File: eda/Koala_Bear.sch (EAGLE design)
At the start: 21 parts

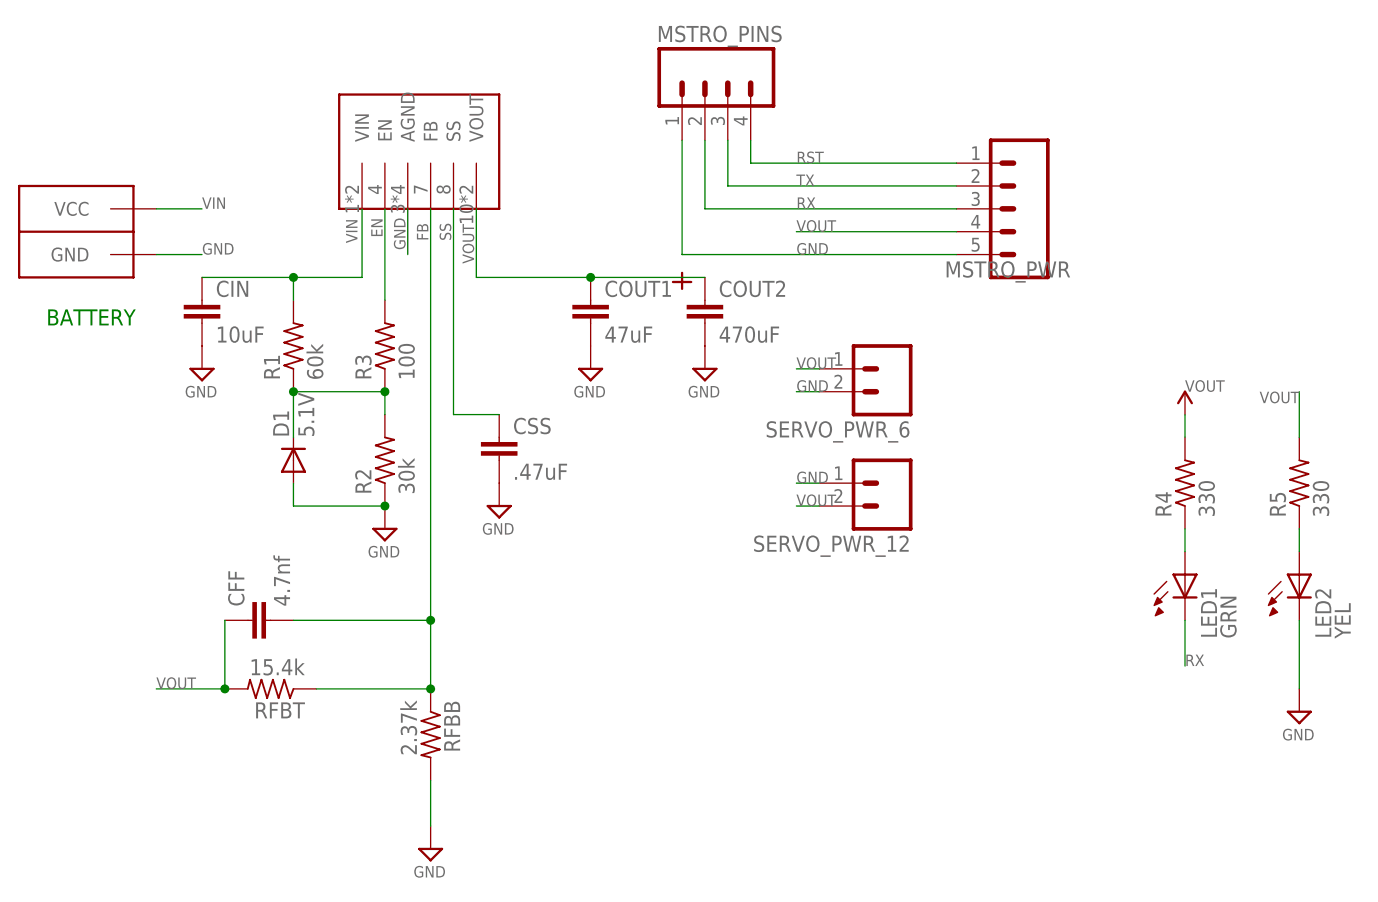
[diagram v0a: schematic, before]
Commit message: Made Koala smaller
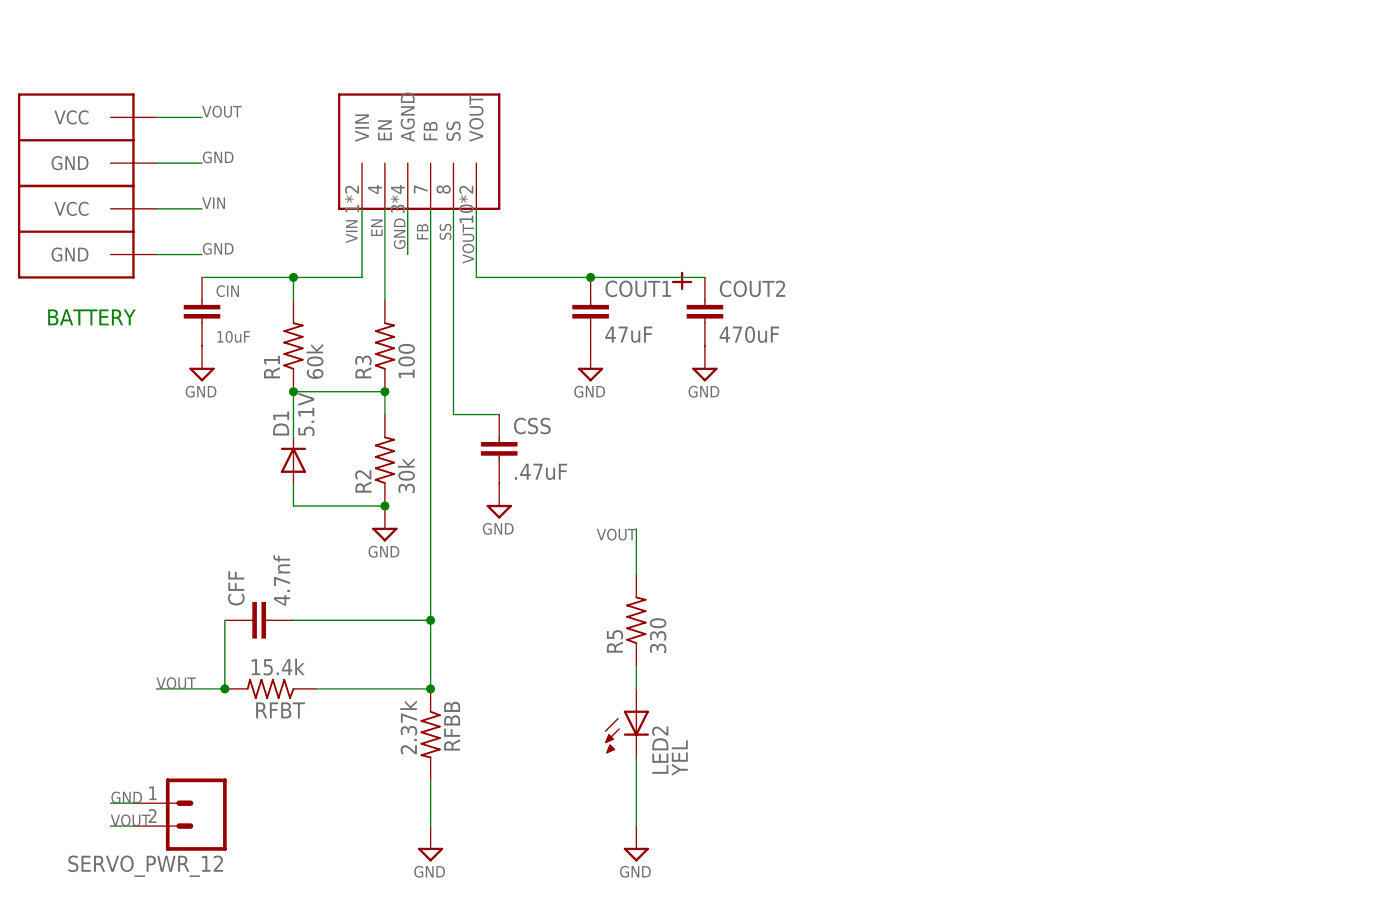
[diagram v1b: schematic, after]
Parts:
- removed LED1: GRN, pie:LED0805
- removed MSTRO_PINS: (no value), pie_new:M041X04-MTA
- removed MSTRO_PWR: (no value), pie:M05MTA
- removed R4: 330, pie:R-US_R0603
- removed SERVO_PWR_6: (no value), pie:M02PTH
- added PWR1: ANDERSONVERTICAL, pie:ANDERSONVERTICAL
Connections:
- removed net N$1: LED1.A, R4.1
- removed net RST: MSTRO_PINS.4, MSTRO_PWR.1
- removed net RX: LED1.C, MSTRO_PINS.2, MSTRO_PWR.3
- removed net TX: MSTRO_PINS.3, MSTRO_PWR.2
- net GND: now also PWR1.GND; no longer MSTRO_PINS.1, MSTRO_PWR.5, SERVO_PWR_6.2
- net VOUT: now also PWR1.VCC; no longer MSTRO_PWR.4, R4.2, SERVO_PWR_6.1
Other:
- moved on the sheet: LED2, R5, SERVO_PWR_12

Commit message: Update a bunch more part metadata
Team flag, smartsensor jig, both smartsensors, and controller now have
complete BOM information.
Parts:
- CIN: device pie:CAP0603-CAP -> pie:CAP1206
- LED2: value YEL -> YELLOW
- R1: value 60k -> 62k
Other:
- moved on the sheet: SERVO_PWR_12
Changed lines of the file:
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@@
 <setting verticaltext="up"/>
 </settings>
-<grid distance="0.1" unitdist="inch" unit="inch" style="lines" multiple="1" display="no" altdistance="0.01" altunitdist="inch" altunit="inch"/>
+<grid distance="0.1" unitdist="inch" unit="inch" style="lines" multiple="1" display="yes" altdistance="0.05" altunitdist="inch" altunit="inch"/>
 <layers>
 <layer number="1" name="Top" color="4" fill="1" visible="no" active="no"/>
+<layer number="2" name="Route2" color="1" fill="3" visible="no" active="no"/>
+<layer number="3" name="Route3" color="4" fill="3" visible="no" active="no"/>
+<layer number="4" name="Route4" color="1" fill="4" visible="no" active="no"/>
+<layer number="5" name="Route5" color="4" fill="4" visible="no" active="no"/>
+<layer number="6" name="Route6" color="1" fill="8" visible="no" active="no"/>
+<layer number="7" name="Route7" color="4" fill="8" visible="no" active="no"/>
+<layer number="8" name="Route8" color="1" fill="2" visible="no" active="no"/>
+<layer number="9" name="Route9" color="4" fill="2" visible="no" active="no"/>
+<layer number="10" name="Route10" color="1" fill="7" visible="no" active="no"/>
+<layer number="11" name="Route11" color="4" fill="7" visible="no" active="no"/>
+<layer number="12" name="Route12" color="1" fill="5" visible="no" active="no"/>
+<layer number="13" name="Route13" color="4" fill="5" visible="no" active="no"/>
+<layer number="14" name="Route14" color="1" fill="6" visible="no" active="no"/>
+<layer number="15" name="Route15" color="4" fill="6" visible="no" active="no"/>
 <layer number="16" name="Bottom" color="1" fill="1" visible="no" active="no"/>
 <layer number="17" name="Pads" color="2" fill="1" visible="no" active="no"/>
@@
 <part name="SUPPLY9" library="supply2" deviceset="GND" device=""/>
 <part name="SUPPLY2" library="supply2" deviceset="GND" device=""/>
-<part name="R1" library="pie" deviceset="R-US_" device="R0603" value="60k"/>
+<part name="R1" library="pie" deviceset="R-US_" device="R0603" value="62k"/>
 <part name="R2" library="pie" deviceset="R-US_" device="R0603" value="30k"/>
 <part name="RFBT" library="pie" deviceset="R-US_" device="R0603" value="15.4k"/>
@@
 <part name="CFF" library="pie" deviceset="CAP" device="0603-CAP" value="4.7nf"/>
 <part name="CSS" library="pie" deviceset="CAP" device="0603-CAP" value=".47uF"/>
-<part name="CIN" library="pie" deviceset="CAP" device="0603-CAP" value="10uF"/>
+<part name="CIN" library="pie" deviceset="CAP" device="1206" value="10uF"/>
 <part name="COUT1" library="SparkFun" deviceset="CAP" device="1206" value="47uF"/>
 <part name="D1" library="SparkFun" deviceset="DIODE" device="SOD" value="5.1V"/>
@@
 </part>
 <part name="R5" library="pie" deviceset="R-US_" device="R0603" value="330"/>
-<part name="LED2" library="pie" deviceset="LED" device="0805" value="YEL"/>
+<part name="LED2" library="pie" deviceset="LED" device="0805" value="YELLOW"/>
 <part name="SUPPLY4" library="supply2" deviceset="GND" device=""/>
 <part name="PWR" library="pie" deviceset="ANDERSON" device="VERTICAL"/>
@@
 <segment>
 <pinref part="SERVO_PWR_12" gate="G$1" pin="1"/>
-<wire x1="-17.78" y1="-20.32" x2="-20.32" y2="-20.32" width="0.1524" layer="91"/>
+<wire x1="-17.78" y1="-17.78" x2="-20.32" y2="-20.32" width="0.1524" layer="91"/>
 <label x="-20.32" y="-20.32" size="1.27" layer="95" font="vector"/>
 </segment>
@@
 <segment>
 <pinref part="SERVO_PWR_12" gate="G$1" pin="2"/>
-<wire x1="-17.78" y1="-22.86" x2="-20.32" y2="-22.86" width="0.1524" layer="91"/>
+<wire x1="-17.78" y1="-20.32" x2="-20.32" y2="-22.86" width="0.1524" layer="91"/>
 <label x="-20.32" y="-22.86" size="1.27" layer="95" font="vector"/>
 </segment>

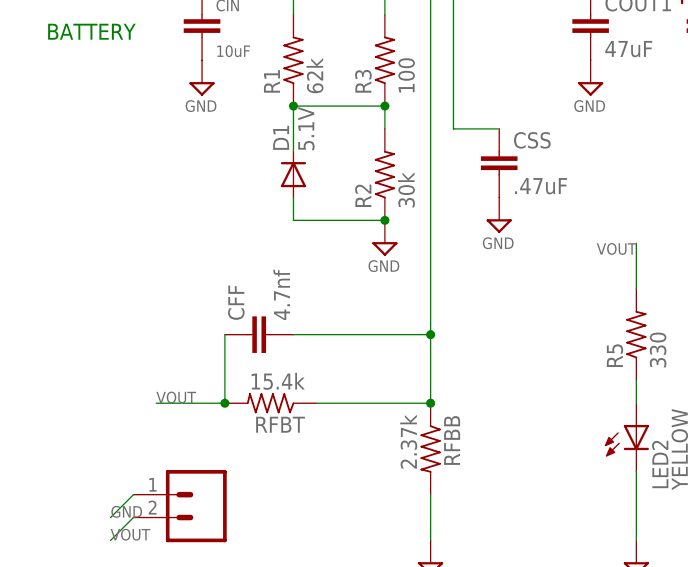
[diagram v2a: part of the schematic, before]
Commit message: Move Koala parts to pie.lbr, update BOM data
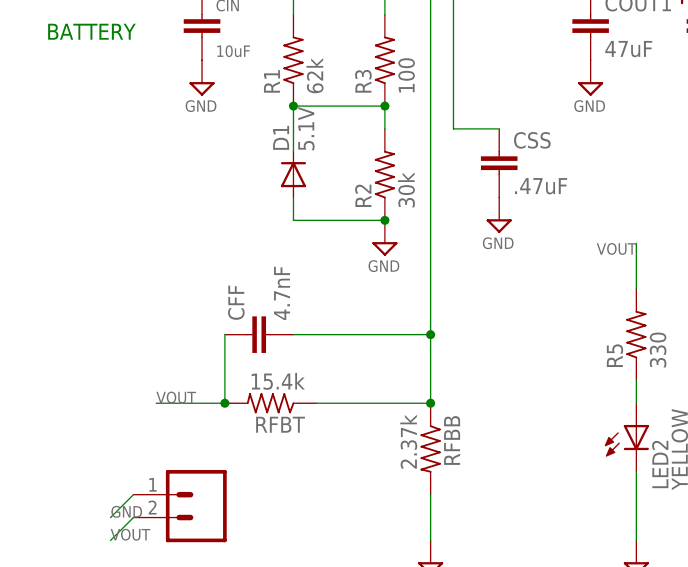
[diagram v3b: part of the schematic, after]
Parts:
- CFF: value 4.7nf -> 4.7nF
- COUT1: device SparkFun:CAP1206 -> pie:CAP1206
- COUT2: device TANT_CASE_E:TANT_CASE_E -> pie:TANT_CASE_E
- D1: device SparkFun:DIODESOD -> pie:DIODESOD-323
- U$1: device LMZ12010:LMZ12010 -> pie:LMZ12010
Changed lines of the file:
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@@
 <part name="SUPPLY7" library="supply2" deviceset="GND" device=""/>
 <part name="SUPPLY8" library="supply2" deviceset="GND" device=""/>
-<part name="U$1" library="LMZ12010" deviceset="LMZ12010" device=""/>
+<part name="U$1" library="pie" deviceset="LMZ12010" device=""/>
 <part name="SUPPLY9" library="supply2" deviceset="GND" device=""/>
 <part name="SUPPLY2" library="supply2" deviceset="GND" device=""/>
@@
 <part name="RFBT" library="pie" deviceset="R-US_" device="R0603" value="15.4k"/>
 <part name="RFBB" library="pie" deviceset="R-US_" device="R0603" value="2.37k"/>
-<part name="CFF" library="pie" deviceset="CAP" device="0603-CAP" value="4.7nf"/>
+<part name="CFF" library="pie" deviceset="CAP" device="0603-CAP" value="4.7nF"/>
 <part name="CSS" library="pie" deviceset="CAP" device="0603-CAP" value=".47uF"/>
 <part name="CIN" library="pie" deviceset="CAP" device="1206" value="10uF"/>
-<part name="COUT1" library="SparkFun" deviceset="CAP" device="1206" value="47uF"/>
-<part name="D1" library="SparkFun" deviceset="DIODE" device="SOD" value="5.1V"/>
-<part name="COUT2" library="TANT_CASE_E" deviceset="TANT_CASE_E" device="" value="470uF"/>
+<part name="COUT1" library="pie" deviceset="CAP" device="1206" value="47uF"/>
+<part name="D1" library="pie" deviceset="DIODE" device="SOD-323" value="5.1V"/>
+<part name="COUT2" library="pie" deviceset="TANT_CASE_E" device="" value="470uF"/>
 <part name="R3" library="pie" deviceset="R-US_" device="R0603" value="100"/>
 <part name="SERVO_PWR_12" library="pie" deviceset="M02" device="PTH"/>
